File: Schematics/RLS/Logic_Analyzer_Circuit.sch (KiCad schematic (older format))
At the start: 2 parts, among them J4 Logic_Analyzer1, J5 Logic_Analyzer2

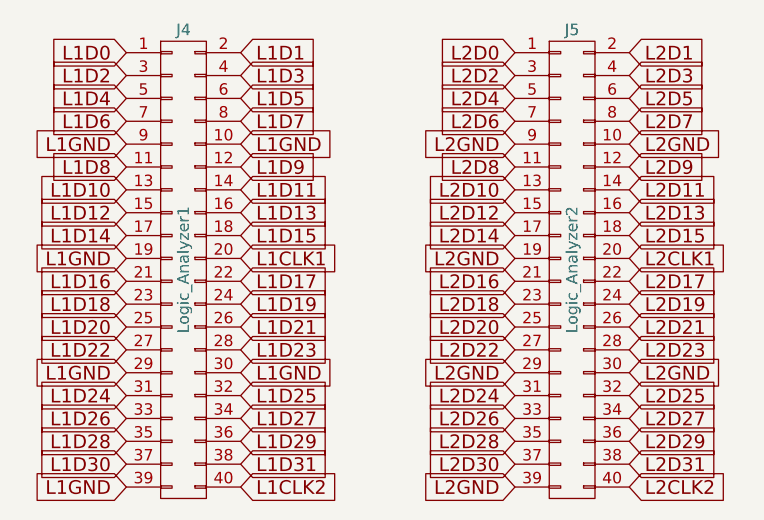
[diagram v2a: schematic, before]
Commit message: Added Things and Fixed Schematic
Added pots to schematic and pcb for adc balancing.
Fixed the component annotation and netlist in the pcb.
Shrunk the pcb down a bit.
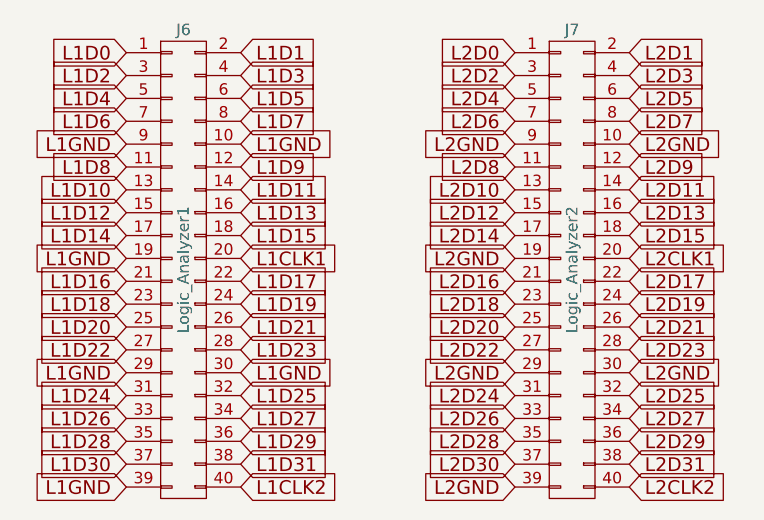
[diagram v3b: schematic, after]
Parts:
- renumbered J4 to J6, J5 to J7
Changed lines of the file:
@@
 $EndDescr
 $Comp
-L CONN_02X20 J4
+L CONN_02X20 J6
 U 1 1 595979EB
 P 4750 3300
-F 0 "J4" H 4750 4350 50  0000 C CNN
+F 0 "J6" H 4750 4350 50  0000 C CNN
 F 1 "Logic_Analyzer1" V 4750 3300 50  0000 C CNN
 F 2 "Pin_Headers:Pin_Header_Straight_2x20_Pitch2.54mm" H 4750 2350 50  0001 C CNN
@@
 $EndComp
 $Comp
-L CONN_02X20 J5
+L CONN_02X20 J7
 U 1 1 59597A25
 P 6450 3300
-F 0 "J5" H 6450 4350 50  0000 C CNN
+F 0 "J7" H 6450 4350 50  0000 C CNN
 F 1 "Logic_Analyzer2" V 6450 3300 50  0000 C CNN
 F 2 "Pin_Headers:Pin_Header_Straight_2x20_Pitch2.54mm" H 6450 2350 50  0001 C CNN
